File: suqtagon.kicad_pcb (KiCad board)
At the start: 2 copper layers, 100 x 86.6 mm, 6 parts

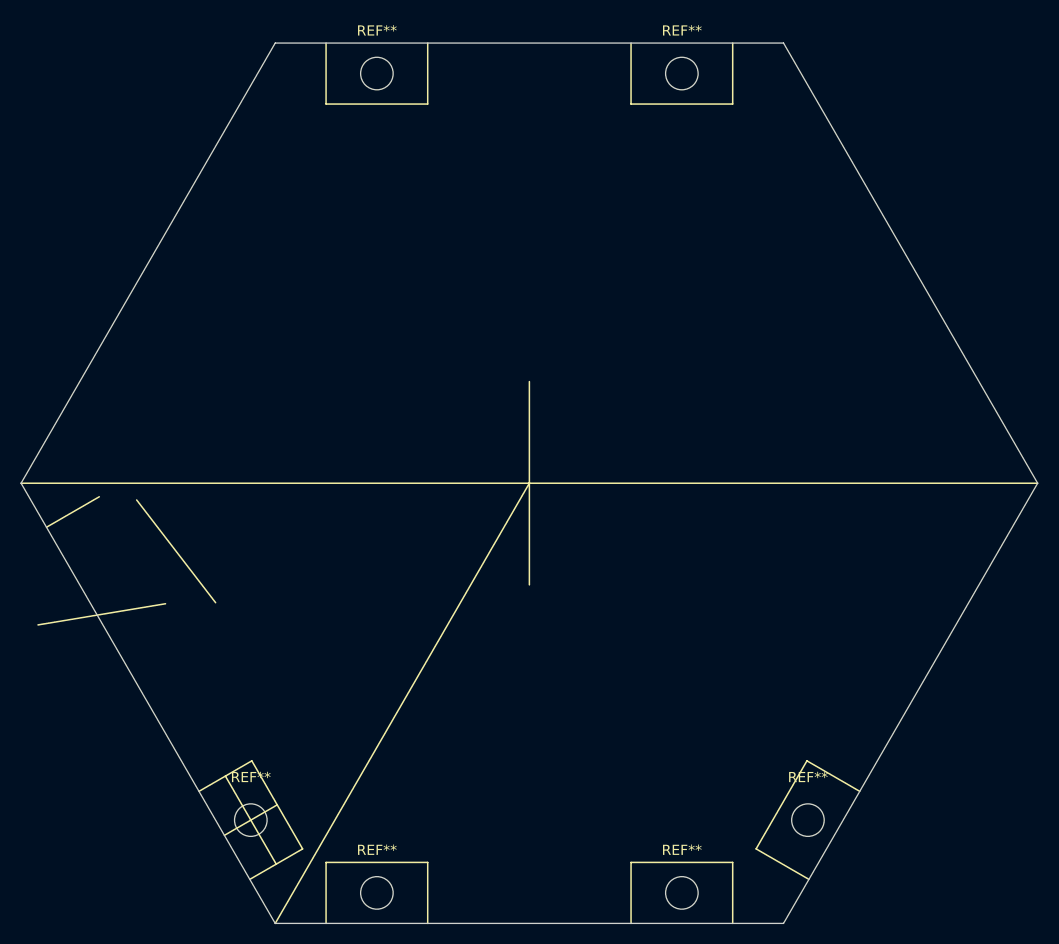
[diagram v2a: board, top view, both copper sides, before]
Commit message: all mount holes placed
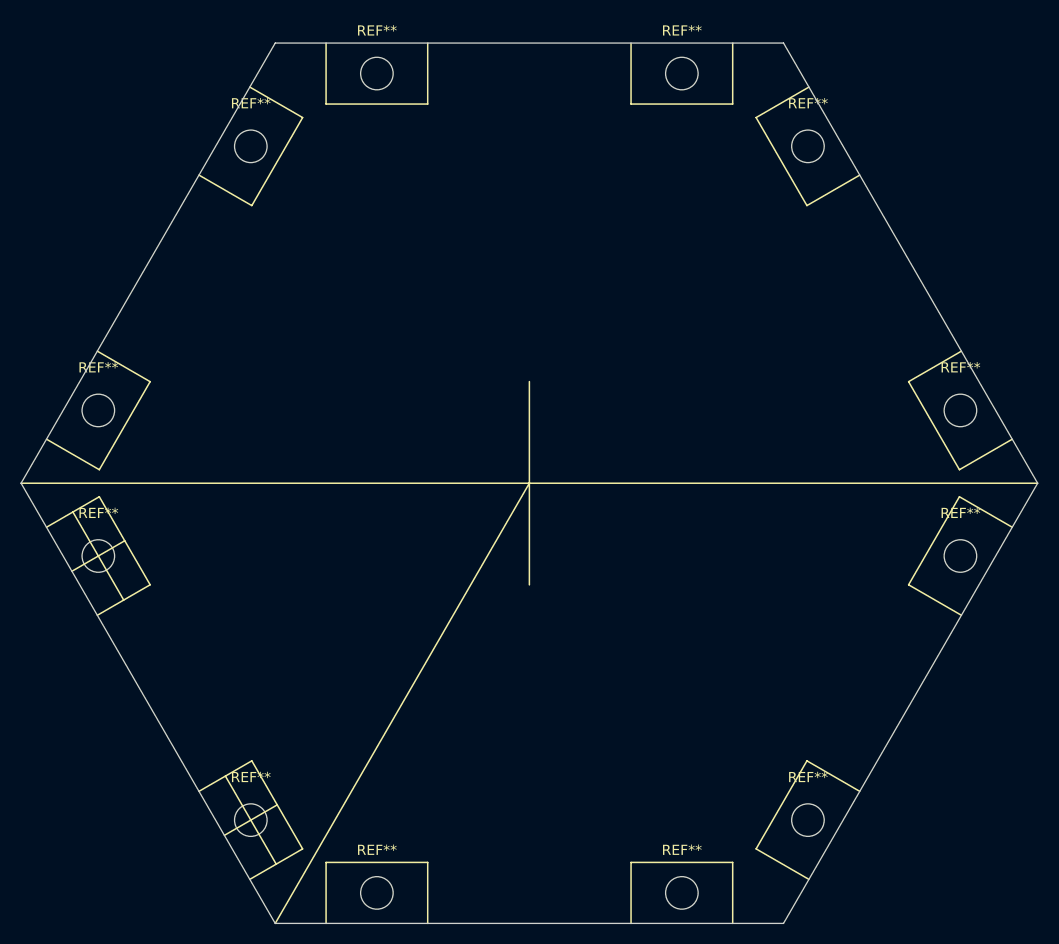
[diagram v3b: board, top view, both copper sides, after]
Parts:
- added REF**: MountingHole_3.2mm_M3, MountingHole:MountingHole_3.2mm_M3, F.Cu at (57.6, 100.5)
- added REF**: MountingHole_3.2mm_M3, MountingHole:MountingHole_3.2mm_M3, F.Cu at (142.4, 100.5)
- added REF**: MountingHole_3.2mm_M3, MountingHole:MountingHole_3.2mm_M3, F.Cu at (57.6, 86.1)
- added REF**: MountingHole_3.2mm_M3, MountingHole:MountingHole_3.2mm_M3, F.Cu at (127.4, 60.2)
- added REF**: MountingHole_3.2mm_M3, MountingHole:MountingHole_3.2mm_M3, F.Cu at (72.6, 60.2)
- added REF**: MountingHole_3.2mm_M3, MountingHole:MountingHole_3.2mm_M3, F.Cu at (142.4, 86.1)
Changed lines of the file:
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@@
+  )
+  (footprint "MountingHole:MountingHole_3.2mm_M3" (layer "F.Cu")
+    (at 57.598 86.14)
+    (descr "Mounting Hole 3.2mm, no annular, M3")
+    (tags "mounting hole 3.2mm no annular m3")
+    (attr exclude_from_pos_files exclude_from_bom)
+    (fp_text reference "REF**" (at 0 -4.2) (layer "F.SilkS")
+      (effects (font (size 1 1) (thickness 0.15)))
+    )
+    (fp_text value "MountingHole_3.2mm_M3" (at 0 4.2) (layer "F.Fab")
+      (effects (font (size 1 1) (thickness 0.15)))
+    )
+    (fp_text user "${REFERENCE}" (at 0 0) (layer "F.Fab")
+      (effects (font (size 1 1) (thickness 0.15)))
+    )
+    (fp_circle (center 0 0) (end 3.2 0) (layer "Cmts.User") (width 0.15) (fill none))
+    (fp_circle (center 0 0) (end 3.45 0) (layer "F.CrtYd") (width 0.05) (fill none))
+    (pad "" np_thru_hole circle (at 0 0) (size 3.2 3.2) (drill 3.2) (layers *.Cu *.Mask))
   )
   (footprint "MountingHole:MountingHole_3.2mm_M3" (layer "F.Cu")
@@
   )
   (footprint "MountingHole:MountingHole_3.2mm_M3" (layer "F.Cu")
+    (at 127.402 60.16)
+    (descr "Mounting Hole 3.2mm, no annular, M3")
+    (tags "mounting hole 3.2mm no annular m3")
+    (attr exclude_from_pos_files exclude_from_bom)
+    (fp_text reference "REF**" (at 0 -4.2) (layer "F.SilkS")
+      (effects (font (size 1 1) (thickness 0.15)))
+    )
+    (fp_text value "MountingHole_3.2mm_M3" (at 0 4.2) (layer "F.Fab")
+      (effects (font (size 1 1) (thickness 0.15)))
+    )
+    (fp_text user "${REFERENCE}" (at 0 0) (layer "F.Fab")
+      (effects (font (size 1 1) (thickness 0.15)))
+    )
+    (fp_circle (center 0 0) (end 3.2 0) (layer "Cmts.User") (width 0.15) (fill none))
+    (fp_circle (center 0 0) (end 3.45 0) (layer "F.CrtYd") (width 0.05) (fill none))
+    (pad "" np_thru_hole circle (at 0 0) (size 3.2 3.2) (drill 3.2) (layers *.Cu *.Mask))
+  )
+  (footprint "MountingHole:MountingHole_3.2mm_M3" (layer "F.Cu")
+    (at 72.598 60.16)
+    (descr "Mounting Hole 3.2mm, no annular, M3")
+    (tags "mounting hole 3.2mm no annular m3")
+    (attr exclude_from_pos_files exclude_from_bom)
+    (fp_text reference "REF**" (at 0 -4.2) (layer "F.SilkS")
+      (effects (font (size 1 1) (thickness 0.15)))
+    )
+    (fp_text value "MountingHole_3.2mm_M3" (at 0 4.2) (layer "F.Fab")
+      (effects (font (size 1 1) (thickness 0.15)))
+    )
+    (fp_text user "${REFERENCE}" (at 0 0) (layer "F.Fab")
+      (effects (font (size 1 1) (thickness 0.15)))
+    )
+    (fp_circle (center 0 0) (end 3.2 0) (layer "Cmts.User") (width 0.15) (fill none))
+    (fp_circle (center 0 0) (end 3.45 0) (layer "F.CrtYd") (width 0.05) (fill none))
+    (pad "" np_thru_hole circle (at 0 0) (size 3.2 3.2) (drill 3.2) (layers *.Cu *.Mask))
+  )
+  (footprint "MountingHole:MountingHole_3.2mm_M3" (layer "F.Cu")
+    (at 142.402 86.14)
+    (descr "Mounting Hole 3.2mm, no annular, M3")
+    (tags "mounting hole 3.2mm no annular m3")
+    (attr exclude_from_pos_files exclude_from_bom)
+    (fp_text reference "REF**" (at 0 -4.2) (layer "F.SilkS")
+      (effects (font (size 1 1) (thickness 0.15)))
+    )
+    (fp_text value "MountingHole_3.2mm_M3" (at 0 4.2) (layer "F.Fab")
+      (effects (font (size 1 1) (thickness 0.15)))
+    )
+    (fp_text user "${REFERENCE}" (at 0 0) (layer "F.Fab")
+      (effects (font (size 1 1) (thickness 0.15)))
+    )
+    (fp_circle (center 0 0) (end 3.2 0) (layer "Cmts.User") (width 0.15) (fill none))
+    (fp_circle (center 0 0) (end 3.45 0) (layer "F.CrtYd") (width 0.05) (fill none))
+    (pad "" np_thru_hole circle (at 0 0) (size 3.2 3.2) (drill 3.2) (layers *.Cu *.Mask))
+  )
+  (footprint "MountingHole:MountingHole_3.2mm_M3" (layer "F.Cu")
     (at 115 133.6)
     (descr "Mounting Hole 3.2mm, no annular, M3")
@@
   )
   (footprint "MountingHole:MountingHole_3.2mm_M3" (layer "F.Cu")
+    (at 57.598 100.46)
+    (descr "Mounting Hole 3.2mm, no annular, M3")
+    (tags "mounting hole 3.2mm no annular m3")
+    (attr exclude_from_pos_files exclude_from_bom)
+    (fp_text reference "REF**" (at 0 -4.2) (layer "F.SilkS")
+      (effects (font (size 1 1) (thickness 0.15)))
+    )
+    (fp_text value "MountingHole_3.2mm_M3" (at 0 4.2) (layer "F.Fab")
+      (effects (font (size 1 1) (thickness 0.15)))
+    )
+    (fp_text user "${REFERENCE}" (at 0 0) (layer "F.Fab")
+      (effects (font (size 1 1) (thickness 0.15)))
+    )
+    (fp_circle (center 0 0) (end 3.2 0) (layer "Cmts.User") (width 0.15) (fill none))
+    (fp_circle (center 0 0) (end 3.45 0) (layer "F.CrtYd") (width 0.05) (fill none))
+    (pad "" np_thru_hole circle (at 0 0) (size 3.2 3.2) (drill 3.2) (layers *.Cu *.Mask))
+  )
+  (footprint "MountingHole:MountingHole_3.2mm_M3" (layer "F.Cu")
+    (at 142.402 100.46)
+    (descr "Mounting Hole 3.2mm, no annular, M3")
+    (tags "mounting hole 3.2mm no annular m3")
+    (attr exclude_from_pos_files exclude_from_bom)
+    (fp_text reference "REF**" (at 0 -4.2) (layer "F.SilkS")
+      (effects (font (size 1 1) (thickness 0.15)))
+    )
+    (fp_text value "MountingHole_3.2mm_M3" (at 0 4.2) (layer "F.Fab")
+      (effects (font (size 1 1) (thickness 0.15)))
+    )
+    (fp_text user "${REFERENCE}" (at 0 0) (layer "F.Fab")
+      (effects (font (size 1 1) (thickness 0.15)))
+    )
+    (fp_circle (center 0 0) (end 3.2 0) (layer "Cmts.User") (width 0.15) (fill none))
+    (fp_circle (center 0 0) (end 3.45 0) (layer "F.CrtYd") (width 0.05) (fill none))
+    (pad "" np_thru_hole circle (at 0 0) (size 3.2 3.2) (drill 3.2) (layers *.Cu *.Mask))
+  )
+  (footprint "MountingHole:MountingHole_3.2mm_M3" (layer "F.Cu")
     (at 127.402 126.44)
     (descr "Mounting Hole 3.2mm, no annular, M3")
@@
   )
   (gr_line (start 127.304 120.61) (end 122.304 129.27) (layer "F.SilkS") (width 0.15))
-  (gr_line (start 51.6636 107.2388) (end 64.2112 105.156) (layer "F.SilkS") (width 0.15))
+  (gr_line (start 57.5 106.29) (end 62.696 103.29) (layer "F.SilkS") (width 0.15))
   (gr_line (start 132.5 123.61) (end 127.304 120.61) (layer "F.SilkS") (width 0.15))
   (gr_line (start 100 83.3) (end 100 103.3) (layer "F.SilkS") (width 0.15))
-  (gr_line (start 61.3664 94.9452) (end 69.1388 105.0544) (layer "F.SilkS") (width 0.15))
+  (gr_line (start 52.5 88.97) (end 57.696 91.97) (layer "F.SilkS") (width 0.15))
+  (gr_line (start 57.696 94.63) (end 62.696 103.29) (layer "F.SilkS") (width 0.15))
+  (gr_line (start 122.304 57.33) (end 127.5 54.33) (layer "F.SilkS") (width 0.15))
   (gr_line (start 90 56) (end 90 50) (layer "F.SilkS") (width 0.15))
+  (gr_line (start 127.304 65.99) (end 122.304 57.33) (layer "F.SilkS") (width 0.15))
   (gr_line (start 50 93.3) (end 150 93.3) (layer "F.SilkS") (width 0.15))
+  (gr_line (start 67.5 62.99) (end 72.696 65.99) (layer "F.SilkS") (width 0.15))
   (gr_line (start 80 136.6) (end 80 130.6) (layer "F.SilkS") (width 0.15))
+  (gr_line (start 142.304 91.97) (end 147.5 88.97) (layer "F.SilkS") (width 0.15))
   (gr_line (start 127.5 132.27) (end 122.304 129.27) (layer "F.SilkS") (width 0.15))
+  (gr_line (start 127.304 65.99) (end 132.5 62.99) (layer "F.SilkS") (width 0.15))
   (gr_line (start 110 56) (end 120 56) (layer "F.SilkS") (width 0.15))
+  (gr_line (start 137.304 103.29) (end 142.5 106.29) (layer "F.SilkS") (width 0.15))
   (gr_line (start 70 127.94) (end 75.196 124.94) (layer "F.SilkS") (width 0.15))
   (gr_line (start 72.696 120.61) (end 77.696 129.27) (layer "F.SilkS") (width 0.15))
   (gr_line (start 80 56) (end 90 56) (layer "F.SilkS") (width 0.15))
+  (gr_line (start 142.304 91.97) (end 137.304 83.31) (layer "F.SilkS") (width 0.15))
+  (gr_line (start 137.304 103.29) (end 142.304 94.63) (layer "F.SilkS") (width 0.15))
+  (gr_line (start 77.696 57.33) (end 72.696 65.99) (layer "F.SilkS") (width 0.15))
   (gr_line (start 52.5 97.63) (end 57.696 94.63) (layer "F.SilkS") (width 0.15))
+  (gr_line (start 142.304 94.63) (end 147.5 97.63) (layer "F.SilkS") (width 0.15))
+  (gr_line (start 57.696 91.97) (end 62.696 83.31) (layer "F.SilkS") (width 0.15))
   (gr_line (start 110 56) (end 110 50) (layer "F.SilkS") (width 0.15))
   (gr_line (start 67.5 123.61) (end 72.696 120.61) (layer "F.SilkS") (width 0.15))
@@
   (gr_line (start 80 130.6) (end 90 130.6) (layer "F.SilkS") (width 0.15))
   (gr_line (start 75 136.6) (end 100 93.3) (layer "F.SilkS") (width 0.15))
+  (gr_line (start 55 101.96) (end 60.196 98.96) (layer "F.SilkS") (width 0.15))
   (gr_line (start 120 136.6) (end 120 130.6) (layer "F.SilkS") (width 0.15))
   (gr_line (start 120 56) (end 120 50) (layer "F.SilkS") (width 0.15))
   (gr_line (start 72.5 132.27) (end 77.696 129.27) (layer "F.SilkS") (width 0.15))
+  (gr_line (start 55.098 96.13) (end 60.098 104.79) (layer "F.SilkS") (width 0.15))
+  (gr_line (start 72.5 54.33) (end 77.696 57.33) (layer "F.SilkS") (width 0.15))
   (gr_line (start 90 136.6) (end 90 130.6) (layer "F.SilkS") (width 0.15))
   (gr_line (start 80 56) (end 80 50) (layer "F.SilkS") (width 0.15))
   (gr_line (start 110 136.6) (end 110 130.6) (layer "F.SilkS") (width 0.15))
+  (gr_line (start 137.304 83.31) (end 142.5 80.31) (layer "F.SilkS") (width 0.15))
+  (gr_line (start 57.5 80.31) (end 62.696 83.31) (layer "F.SilkS") (width 0.15))
   (gr_line (start 75 50) (end 125 50) (layer "Edge.Cuts") (width 0.1))
   (gr_line (start 125 136.6) (end 150 93.3) (layer "Edge.Cuts") (width 0.1))

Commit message: 1204 smd side led footprint created
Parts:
- added D1: LED_RGBA, LED_SMD_SIDE:LED_RGB_1210, F.Cu at (102.2, 131.2)
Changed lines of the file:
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@@
   )
   (net 0 "")
+  (net 1 "unconnected-(D1-Pad1)")
+  (net 2 "unconnected-(D1-Pad2)")
+  (net 3 "unconnected-(D1-Pad3)")
+  (net 4 "unconnected-(D1-Pad4)")
   (footprint "MountingHole:MountingHole_3.2mm_M3" (layer "F.Cu")
     (at 115 53)
@@
     (fp_circle (center 0 0) (end 3.45 0) (layer "F.CrtYd") (width 0.05) (fill none))
     (pad "" np_thru_hole circle (at 0 0) (size 3.2 3.2) (drill 3.2) (layers *.Cu *.Mask))
+  )
+  (footprint "LED_SMD_SIDE:LED_RGB_1210" (layer "F.Cu")
+    (at 102.1588 131.1656)
+    (descr "RGB LED 3.2x2.7mm http://www.avagotech.com/docs/AV02-0610EN")
+    (tags "LED 3227")
+    (property "Sheetfile" "suqtagon.kicad_sch")
+    (property "Sheetname" "")
+    (attr smd)
+    (fp_text reference "D1" (at 0 -2.3) (layer "F.SilkS")
+      (effects (font (size 1 1) (thickness 0.15)))
+    )
+    (fp_text value "LED_RGBA" (at 0 2.45) (layer "F.Fab")
+      (effects (font (size 1 1) (thickness 0.15)))
+    )
+    (fp_text user "${REFERENCE}" (at 0 -2.3) (layer "F.Fab")
+      (effects (font (size 1 1) (thickness 0.15)))
+    )
+    (fp_line (start 1.95 -1.55) (end -1.95 -1.55) (layer "F.SilkS") (width 0.15))
+    (fp_line (start -1.95 -0.5) (end -1.95 -1.55) (layer "F.SilkS") (width 0.15))
+    (fp_line (start 1.95 0.725) (end -1.95 0.725) (layer "F.SilkS") (width 0.15))
+    (fp_line (start 2.1 -1.7) (end -2.1 -1.7) (layer "F.CrtYd") (width 0.05))
+    (fp_line (start -2.1 0.875) (end 2.1 0.875) (layer "F.CrtYd") (width 0.05))
+    (fp_line (start 2.1 0.875) (end 2.1 -1.7) (layer "F.CrtYd") (width 0.05))
+    (fp_line (start -2.1 -1.7) (end -2.1 0.875) (layer "F.CrtYd") (width 0.05))
+    (fp_line (start -1.6 -0.25) (end 1.6 -0.25) (layer "F.Fab") (width 0.1))
+    (fp_line (start -1.6 0.25) (end -1.6 -0.25) (layer "F.Fab") (width 0.1))
+    (fp_line (start 1.6 0.25) (end -1.6 0.25) (layer "F.Fab") (width 0.1))
+    (fp_line (start 1.6 -0.25) (end 1.6 0.25) (layer "F.Fab") (width 0.1))
+    (fp_arc (start -1 -0.25) (mid 0 -1.25) (end 1 -0.25) (layer "F.Fab") (width 0.1))
+    (pad "1" smd rect (at -1.3 -0.125 180) (size 0.7 0.6) (layers "F.Cu" "F.Paste" "F.Mask")
+      (net 1 "unconnected-(D1-Pad1)") (pinfunction "RK") (pintype "passive"))
+    (pad "2" smd rect (at -0.375 0.175 180) (size 0.45 0.5) (layers "F.Cu" "F.Paste" "F.Mask")
+      (net 2 "unconnected-(D1-Pad2)") (pinfunction "GK") (pintype "passive"))
+    (pad "3" smd rect (at 0.375 0.175 180) (size 0.45 0.5) (layers "F.Cu" "F.Paste" "F.Mask")
+      (net 3 "unconnected-(D1-Pad3)") (pinfunction "BK") (pintype "passive"))
+    (pad "4" smd rect (at 1.3 -0.125 180) (size 0.7 0.6) (layers "F.Cu" "F.Paste" "F.Mask")
+      (net 4 "unconnected-(D1-Pad4)") (pinfunction "A") (pintype "passive"))
   )
   (footprint "MountingHole:MountingHole_3.2mm_M3" (layer "F.Cu")
@@
   (gr_line (start 137.304 83.31) (end 142.5 80.31) (layer "F.SilkS") (width 0.15))
   (gr_line (start 57.5 80.31) (end 62.696 83.31) (layer "F.SilkS") (width 0.15))
+  (gr_poly
+    (pts
+      (xy 104.1908 130.8608)
+      (xy 99.9744 130.9116)
+      (xy 95.017788 119.982676)
+      (xy 110.206988 119.881076)
+    ) (layer "F.Mask") (width 0.15) (fill solid))
   (gr_line (start 75 50) (end 125 50) (layer "Edge.Cuts") (width 0.1))
   (gr_line (start 125 136.6) (end 150 93.3) (layer "Edge.Cuts") (width 0.1))
